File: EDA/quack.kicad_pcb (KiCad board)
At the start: 2 copper layers, 56.6 x 57.7 mm, 38 parts, among them IC1 ESP32-PICO-D4, IC2 SN74LVC4245APWR, J1 DIN-4, J2 DB9_Male, J3 FTDI, J4 MODE, U1 AMS1117-3.3, U2 74LVC2T45DC

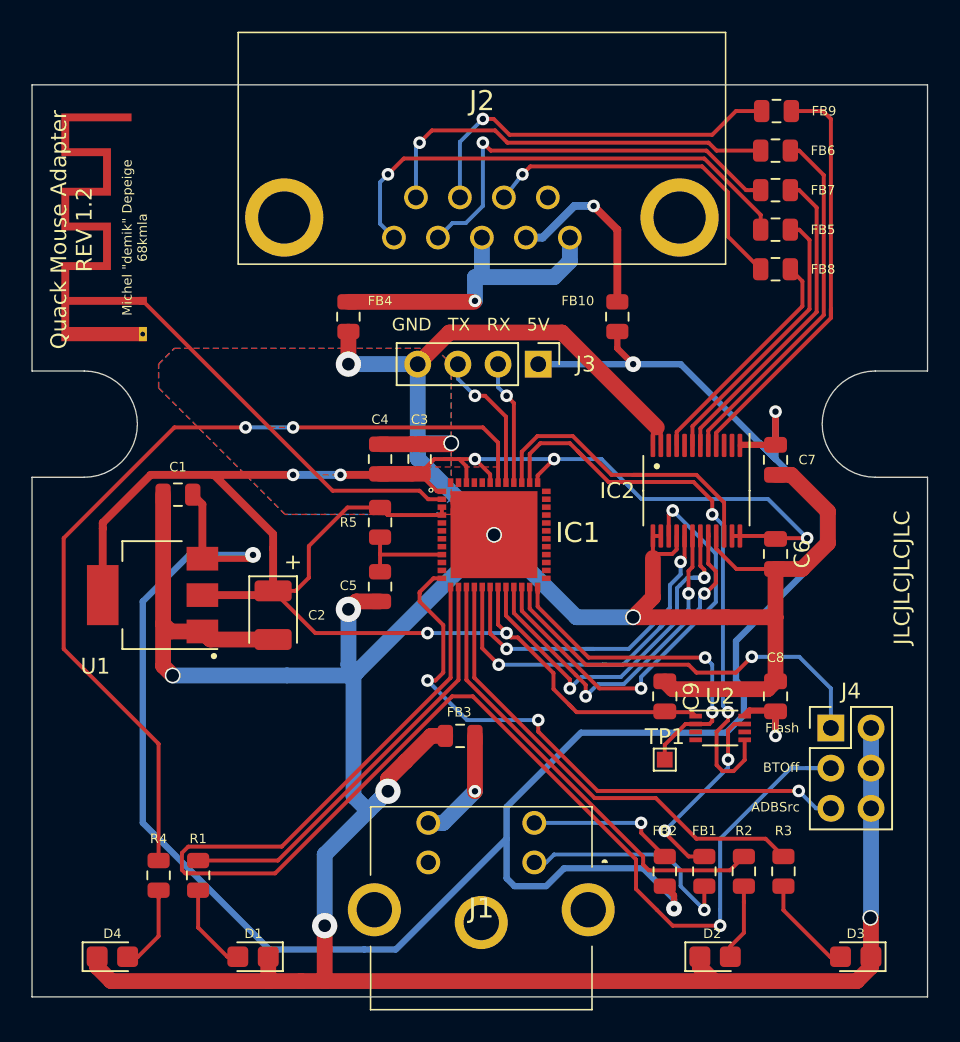
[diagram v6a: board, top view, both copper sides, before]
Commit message: mix fixes: silk, routing, 3D shapes
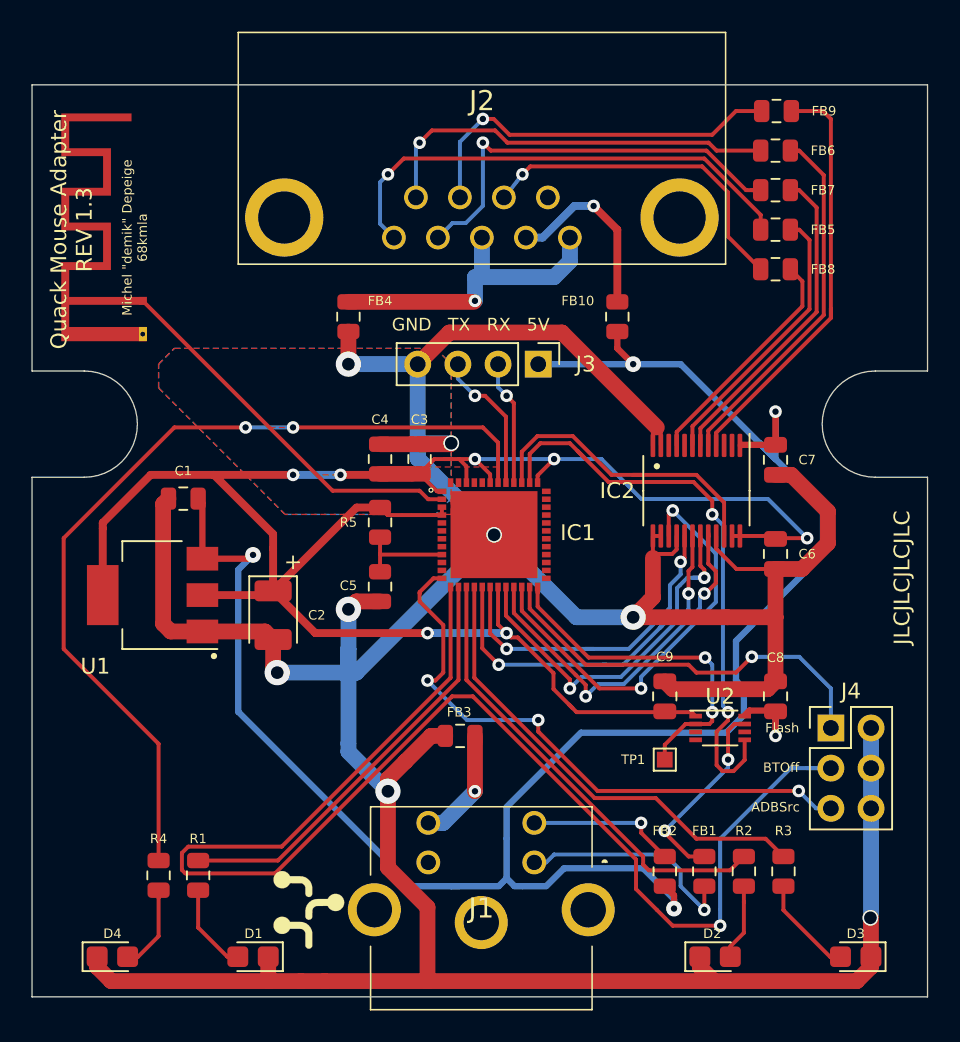
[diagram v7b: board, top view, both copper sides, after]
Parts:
- added G***: LOGO, ADB_logo_5mm:ADB_logo_5mm, F.Cu at (144.5, 121.5)
- moved C1 0.42 mm to (136.6, 95.5)
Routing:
- net +5V: track 149.3 -> 130.1 mm
- net GND: track 255.1 -> 246.3 mm, vias 9 -> 8
- net +3V3: track 128.1 -> 127.0 mm
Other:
- board text added: "Quack Mouse Adapter REV 1.3"
- board text removed: "Quack Mouse Adapter REV 1.2"

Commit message: fixed quad transceiver footprint + reduce led brightness
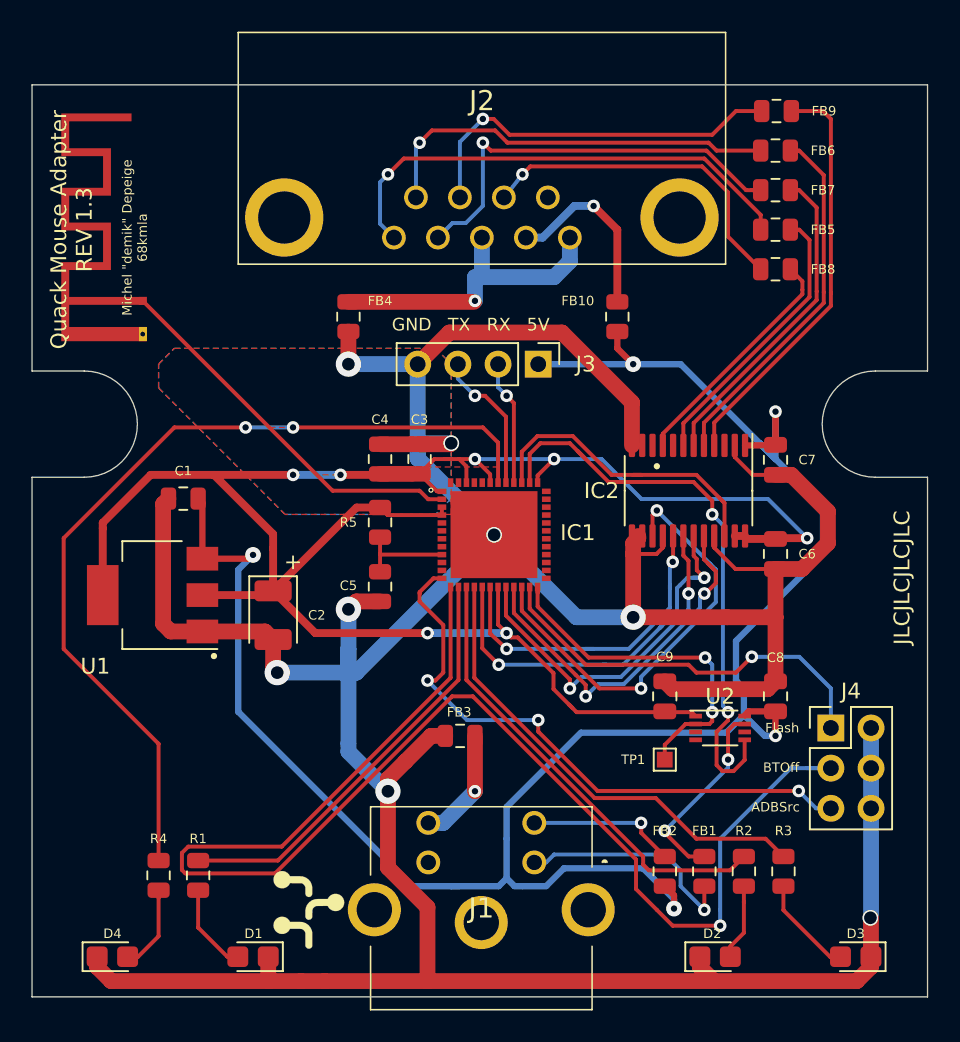
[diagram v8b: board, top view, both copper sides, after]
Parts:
- C3: value 10 -> 10uF
- C4: value 0.1 -> 100nF
- IC2: footprint Package_SO:TSSOP-24_4.4x6.5mm_P0.5mm -> Package_SO:TSSOP-24_4.4x7.8mm_P0.65mm
- moved IC2 0.50 mm to (168.5, 95.0)
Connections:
- IC2 pad 2: (no net) -> GND
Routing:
- net GND: track 246.3 -> 248.1 mm
- net +5V: track 130.1 -> 130.8 mm
